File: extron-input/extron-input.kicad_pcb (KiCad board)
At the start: 2 copper layers, 92 x 37 mm, 24 parts, among them J1 SCART-F, J10 Conn_01x01, J11 Conn_01x01, J12 RED, J13 GREEN, J14 BLUE, J15 SYNC, J2 RED, J3 GREEN, J4 BLUE, J5 SYNC, J6 PHOENIX, J7 SENSE, J8 Conn_01x01, J9 Conn_01x01, SW1 SW_DPDT_x2, U1 LM1881

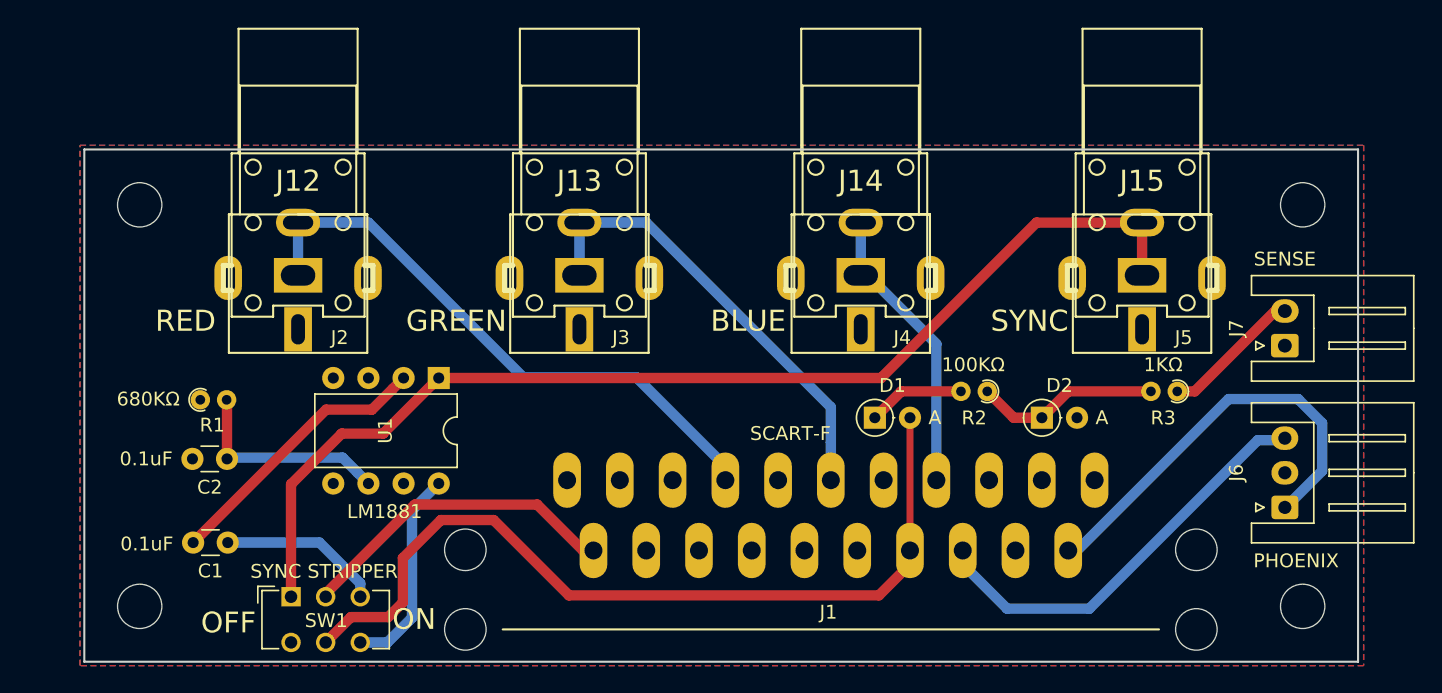
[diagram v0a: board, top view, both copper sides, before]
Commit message: Rev 2.1
Fixed up rca problems by making combined footprint for the two different
CUI-style connectors.
Shifted scart over so it doesn't run into standoffs (hopefully)
Fixed resistor value in sense circuit
Reversed stereo audio signals
Added logos + link to site
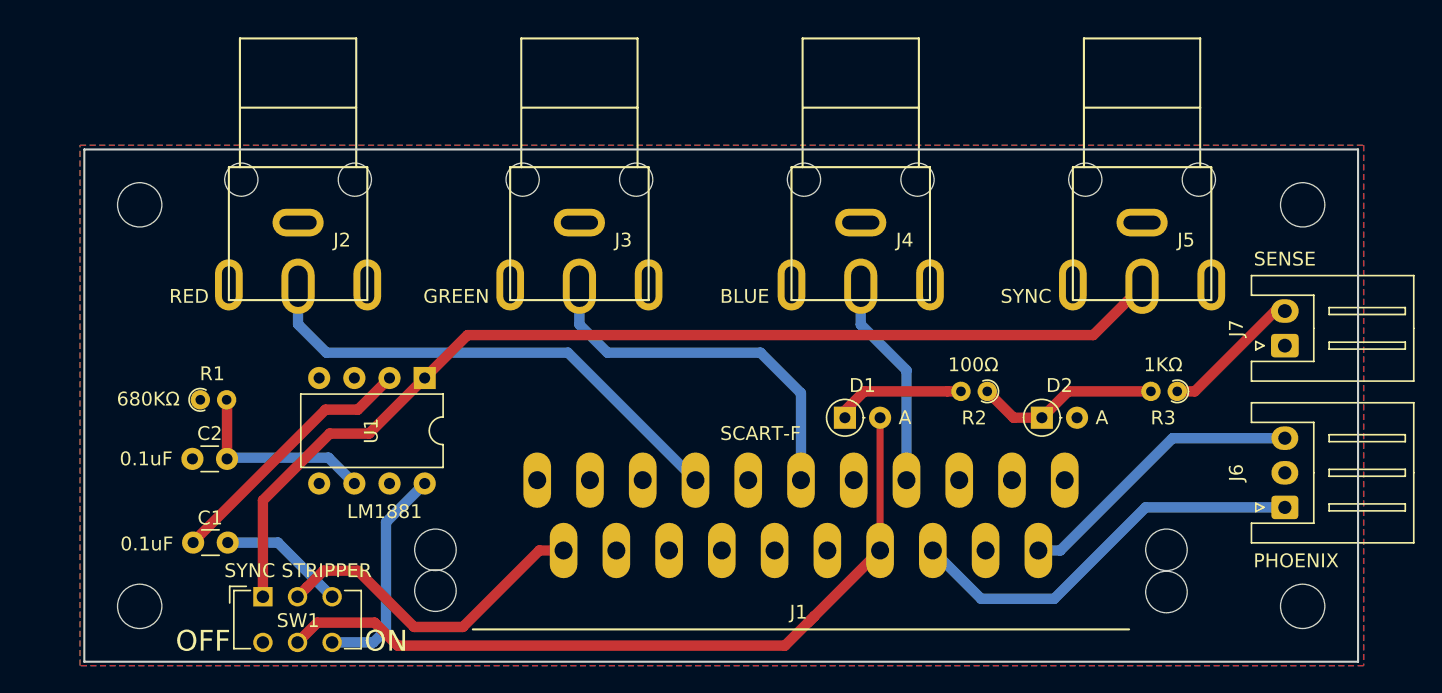
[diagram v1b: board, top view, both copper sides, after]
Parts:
- removed J12: RED, extron-input:rca_black
- removed J13: GREEN, extron-input:rca_black
- removed J14: BLUE, extron-input:rca_black
- removed J15: SYNC, extron-input:rca_black
- added REF**: KiCad-Logo_5mm_SilkScreen, Symbol:KiCad-Logo_5mm_SilkScreen, B.Cu at (111.8, 92.7)
- added REF**: OSHW-Logo_7.5x8mm_SilkScreen, Symbol:OSHW-Logo_7.5x8mm_SilkScreen, B.Cu at (124.5, 92.7)
- J2, J3, J4, J5: footprint extron-input:rca_boom -> extron-input:rca_combined
- R2: value 100KΩ -> 100Ω
- moved J2 3.81 mm to (91.4, 81.3)
- moved J3 3.81 mm to (111.8, 81.3)
- moved J4 3.81 mm to (132.1, 81.3)
- moved J5 3.81 mm to (152.4, 81.3)
- moved D1 2.16 mm to (130.9, 95.4)
- moved J1 2.16 mm to (127.8, 105.0)
- moved SW1 2.03 mm to (88.9, 108.3)
- moved U1 1.02 mm to (100.6, 92.5)
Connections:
- J2 pad 1: RED -> GND
- J2 pad 2: GND -> RED
- J3 pad 1: GREEN -> GND
- J3 pad 2: GND -> GREEN
- J4 pad 1: BLUE -> GND
- J4 pad 2: GND -> BLUE
- J5 pad 1: SYNC -> GND
- J5 pad 2: GND -> SYNC
- J6 pad 1: Net-(J1-Pad2) -> Net-(J1-Pad6)
- J6 pad 3: Net-(J1-Pad6) -> Net-(J1-Pad2)
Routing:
- net Net-(J1-Pad2): track 31.1 -> 21.2 mm
- net RED: track 43.0 -> 36.1 mm
- net GREEN: track 33.8 -> 27.1 mm
- net BLUE: track 20.9 -> 15.4 mm
- net SENSE: track 61.5 -> 56.5 mm
- net SYNC: track 81.2 -> 76.9 mm
- net Net-(C1-Pad1): track 11.8 -> 9.16 mm
- net Net-(D1-Pad1): track 7.01 -> 9.47 mm
- net Net-(SW1-Pad6): track 15.0 -> 16.0 mm
- net Net-(C2-Pad1): track 15.3 -> 14.3 mm
- net Net-(C1-Pad2): track 20.1 -> 19.1 mm
- net Net-(J1-Pad6): track 30.4 -> 29.7 mm
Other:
- board text added: "https://github.com/rattboi/extron-scart-adapter/"

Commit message: Update extron output board to use combined RCA (v2.1)
Small fixes for extron input as well (v2.1)
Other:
- board text added: "v2.1"
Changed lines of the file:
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@@
   (general
     (thickness 1.6)
-    (drawings 9)
+    (drawings 10)
     (tracks 68)
     (zones 0)
@@
   )
   (setup
-    (last_trace_width 0.75)
+    (last_trace_width 0.254)
     (user_trace_width 0.5)
     (user_trace_width 0.75)
@@
     (pad 1 thru_hole oval (at 5 -4.5 180) (size 2 3.7) (drill oval 1 2.7) (layers *.Cu *.Mask)
       (net 1 GND))
+    (model ${KIPRJMOD}/3d_models/rca_black.wrl
+      (at (xyz 0 0 0))
+      (scale (xyz 1 1 1))
+      (rotate (xyz 0 0 0))
+    )
   )
   (module extron-input:rca_combined (layer F.Cu)
@@
     (pad 1 thru_hole oval (at 5 -4.5 180) (size 2 3.7) (drill oval 1 2.7) (layers *.Cu *.Mask)
       (net 1 GND))
+    (model ${KIPRJMOD}/3d_models/rca_black.wrl
+      (at (xyz 0 0 0))
+      (scale (xyz 1 1 1))
+      (rotate (xyz 0 0 0))
+    )
   )
   (module extron-input:rca_combined (layer F.Cu)
@@
     (pad 1 thru_hole oval (at 5 -4.5 180) (size 2 3.7) (drill oval 1 2.7) (layers *.Cu *.Mask)
       (net 1 GND))
+    (model ${KIPRJMOD}/3d_models/rca_black.wrl
+      (at (xyz 0 0 0))
+      (scale (xyz 1 1 1))
+      (rotate (xyz 0 0 0))
+    )
   )
   (module extron-input:rca_combined (layer F.Cu)
@@
     (pad 1 thru_hole oval (at 5 -4.5 180) (size 2 3.7) (drill oval 1 2.7) (layers *.Cu *.Mask)
       (net 1 GND))
+    (model ${KIPRJMOD}/3d_models/rca_black.wrl
+      (at (xyz 0 0 0))
+      (scale (xyz 1 1 1))
+      (rotate (xyz 0 0 0))
+    )
   )
   (module Resistor_THT:R_Axial_DIN0204_L3.6mm_D1.6mm_P1.90mm_Vertical (layer F.Cu)
@@
     )
   )
+  (gr_text v2.1 (at 78.359 111.506) (layer B.SilkS)
+    (effects (font (size 1 1) (thickness 0.25)) (justify mirror))
+  )
   (gr_text "https://github.com/rattboi/extron-scart-adapter/\n" (at 126.492 110.49) (layer B.SilkS)

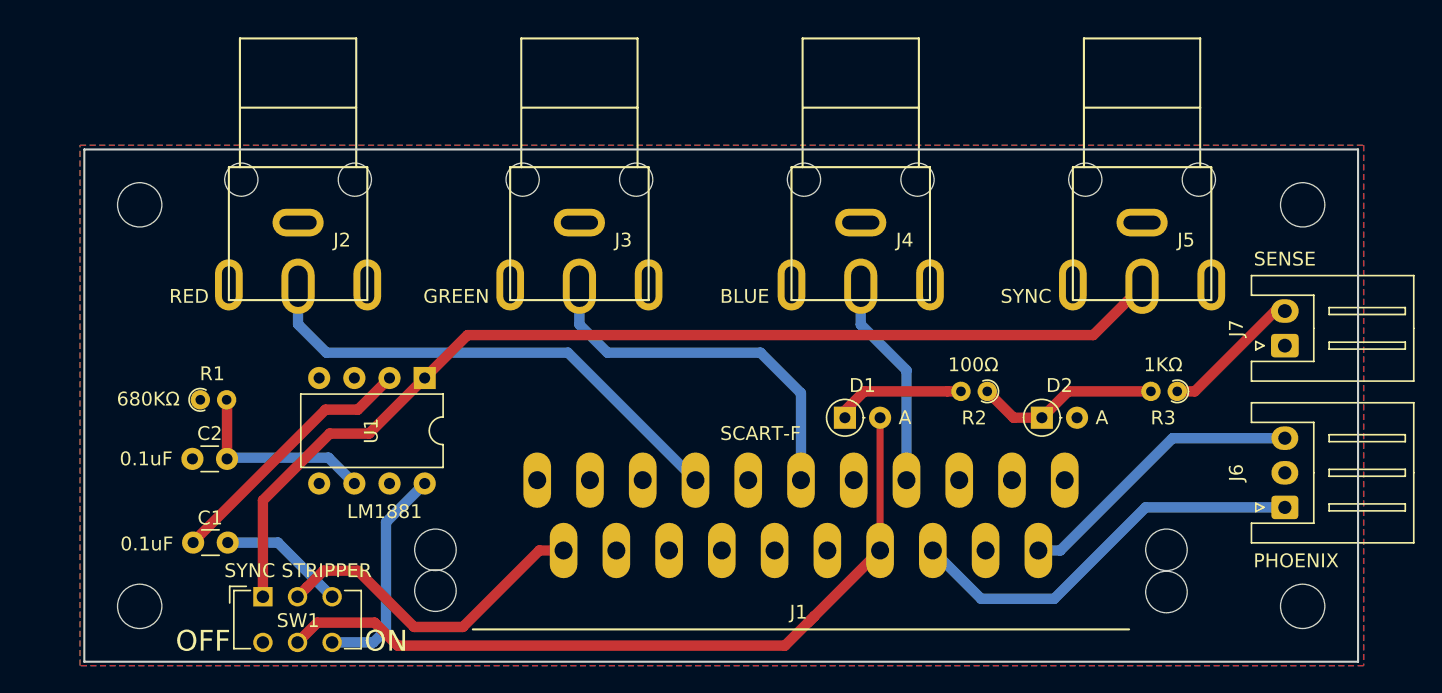
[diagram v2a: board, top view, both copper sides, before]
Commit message: Version 2.2 of extron input (move sense to top)
This revision moves the sense circuit to the top of the board, which
makes the audio plug a lot easier to get at, and you can throw your
esp32-switcher on the top of your extron.

Also cleaned up rescue files for eeschema. Come on, eeschema. Get your
shit together.
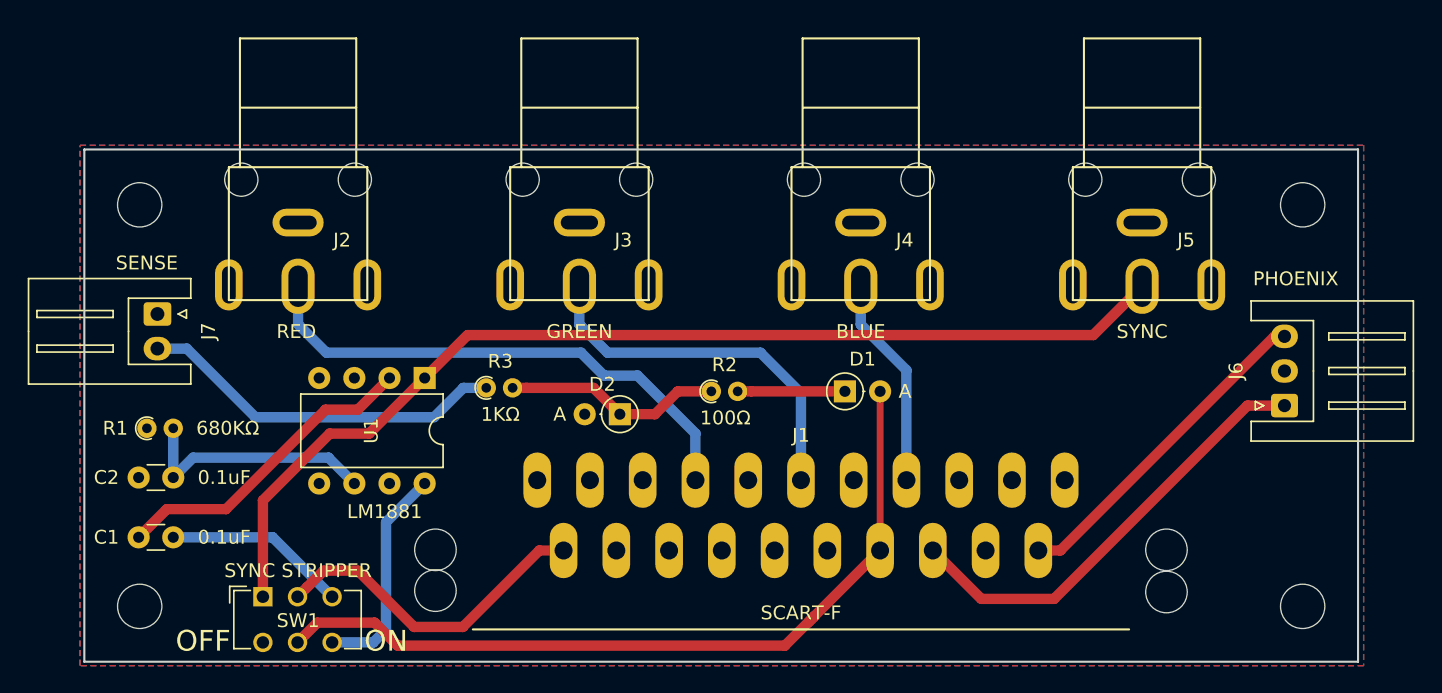
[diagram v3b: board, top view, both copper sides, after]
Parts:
- moved J7 81.5 mm to (81.3, 87.9), turned to 270 degrees
- moved R3 49.9 mm to (105.0, 93.2), turned to 0 degrees
- moved REF** 37.6 mm to (160.8, 102.5)
- moved REF** 34.4 mm to (146.2, 92.8)
- moved D2 30.5 mm to (114.7, 95.1), turned to 180 degrees
- moved R2 19.9 mm to (121.3, 93.5), turned to 0 degrees
- moved J6 7.35 mm to (162.7, 94.5)
- moved R1 4.37 mm to (80.5, 96.1)
- moved C2 4.11 mm to (82.4, 99.7)
- moved C1 3.96 mm to (82.4, 104.0)
- moved D1 1.91 mm to (130.9, 93.5)
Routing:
- net Net-(J7-Pad2): track 10.2 -> 26.7 mm
- net Net-(C1-Pad1): track 9.16 -> 13.3 mm
- net Net-(C1-Pad2): track 19.1 -> 22.9 mm
- net Net-(C2-Pad1): track 14.3 -> 18.0 mm
- net Net-(J1-Pad2): track 21.2 -> 24.2 mm
- net Net-(J1-Pad6): track 29.7 -> 32.6 mm
- net Net-(D2-Pad1): track 13.4 -> 15.8 mm
- net RED: track 36.1 -> 38.1 mm
- net SENSE: track 56.5 -> 58.4 mm
- net Net-(D1-Pad1): track 9.47 -> 7.75 mm
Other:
- board text added: "v2.2"
- board text removed: "v2.1"
